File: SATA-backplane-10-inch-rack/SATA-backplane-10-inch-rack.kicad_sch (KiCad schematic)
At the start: 17 parts, among them J101 Conn_01x06, Q101 DMG1012UW, Q102 DMG1012UW

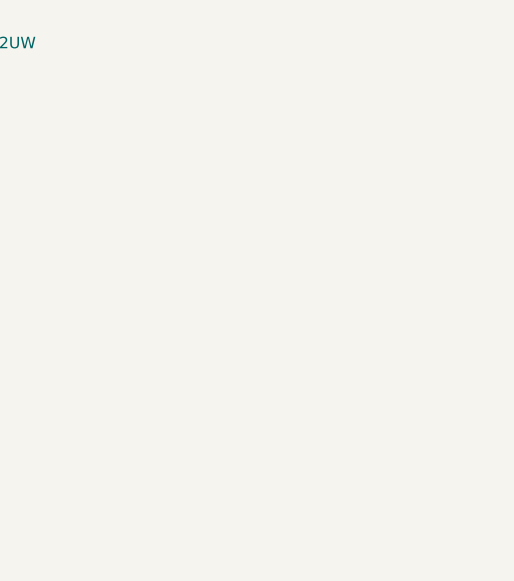
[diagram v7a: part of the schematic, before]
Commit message: Align outline and mounting holes with Jeppe
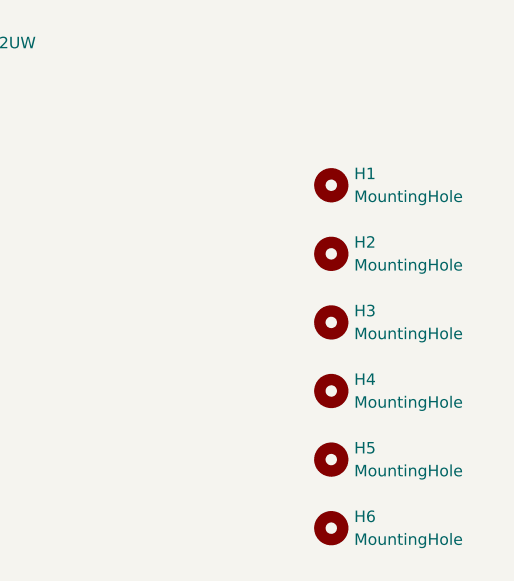
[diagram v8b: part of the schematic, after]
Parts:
- added H1, H2, H3, H4, H5, H6: MountingHole, MountingHole:MountingHole_3.7mm, symbol Mechanical:MountingHole
